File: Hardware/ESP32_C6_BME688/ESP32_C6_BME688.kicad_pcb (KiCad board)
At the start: 2 copper layers, 31.7 x 20 mm, 13 parts, among them J1 USB_C, J2 JST_PH_2PIN, J3 Daughterboard_Interface, U1 ESP32-C6-MINI-1, U3 MCP73831, U4 AP2112K-3.3

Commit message: working POC 1
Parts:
- moved R3 0.80 mm to (129.0, 102.0)
- moved R4 0.80 mm to (129.0, 105.5)
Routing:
- net CC1: track 15.6 -> 14.6 mm
- net GND: track 58.2 -> 57.5 mm
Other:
- board size 31.7 x 20 mm -> 30.8 x 20 mm
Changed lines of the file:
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@@
 	(footprint "Resistor_SMD:R_0603_1608Metric"
 		(layer "F.Cu")
-		(at 129.8 102 90)
+		(at 129 102 90)
 		(descr "Resistor SMD 0603 (1608 Metric), square (rectangular) end terminal, IPC-7351 nominal, (Body size source: IPC-SM-782 page 72, https://www.pcb-3d.com/wordpress/wp-content/uploads/ipc-sm-782a_amendment_1_and_2.pdf)")
 		(tags "resistor")
@@
 	(footprint "Resistor_SMD:R_0603_1608Metric"
 		(layer "F.Cu")
-		(at 129.8 105.5 90)
+		(at 129 105.5 90)
 		(descr "Resistor SMD 0603 (1608 Metric), square (rectangular) end terminal, IPC-7351 nominal, (Body size source: IPC-SM-782 page 72, https://www.pcb-3d.com/wordpress/wp-content/uploads/ipc-sm-782a_amendment_1_and_2.pdf)")
 		(tags "resistor")
@@
 			)
 		)
+		(model "${KICAD10_3DMODEL_DIR}/RF_Module.3dshapes/ESP32-C3-WROOM-02.step"
+			(hide yes)
+			(offset
+				(xyz 0 0 0)
+			)
+			(scale
+				(xyz 1 1 1)
+			)
+			(rotate
+				(xyz 0 0 0)
+			)
+		)
 	)
 	(footprint "Resistor_SMD:R_0603_1608Metric"
@@
 			)
 		)
+		(model "${KICAD10_3DMODEL_DIR}/Connector_USB.3dshapes/USB_C_Receptacle_GCT_USB4105-xx-A_16P_TopMnt_Horizontal.step"
+			(offset
+				(xyz 0 0 0)
+			)
+			(scale
+				(xyz 1 1 1)
+			)
+			(rotate
+				(xyz 0 0 0)
+			)
+		)
 	)
 	(gr_line
 		(start 100 100)
-		(end 131.699999 100)
+		(end 130.75 100)
 		(stroke
 			(width 0.1)
-			(type default)
+			(type solid)
 		)
 		(layer "Edge.Cuts")
@@
 	)
 	(gr_line
-		(start 131.699999 100)
-		(end 131.699999 120)
+		(start 130.75 100)
+		(end 130.75 120)
 		(stroke
 			(width 0.1)
-			(type default)
+			(type solid)
 		)
 		(layer "Edge.Cuts")
 	)
 	(gr_line
-		(start 131.699999 120)
+		(start 130.75 120)
 		(end 100 120)
 		(stroke
 			(width 0.1)
-			(type default)
+			(type solid)
 		)
 		(layer "Edge.Cuts")
@@
 	)
 	(segment
-		(start 123.6683 118.25)
-		(end 118.825 118.25)
+		(start 130.2 105.875)
+		(end 129 104.675)
 		(width 0.2)
 		(layer "F.Cu")
@@
 	)
 	(segment
-		(start 129.14 109.68)
-		(end 130.2917 109.68)
+		(start 123.6683 118.25)
+		(end 118.825 118.25)
 		(width 0.2)
 		(layer "F.Cu")
@@
 	)
 	(segment
-		(start 130.8329 102.2079)
-		(end 129.8 101.175)
-		(width 0.2)
-		(layer "F.Cu")
-		(net "GND")
-	)
-	(segment
 		(start 107.4 107.3)
 		(end 106.8 107.3)
@@
 	)
 	(segment
-		(start 130.576 103.8179)
-		(end 130.576 103.2144)
-		(width 0.15)
-		(layer "F.Cu")
-		(net "GND")
-	)
-	(segment
 		(start 102.5746 108.0729)
 		(end 105.175 108.0729)
@@
 	)
 	(segment
-		(start 130.2917 109.68)
-		(end 130.5775 109.3942)
+		(start 130.2 108.62)
+		(end 130.2 105.875)
 		(width 0.2)
 		(layer "F.Cu")
@@
 	)
 	(segment
-		(start 130.576 103.899)
-		(end 130.576 103.8179)
+		(start 130.2 102.375)
+		(end 129 101.175)
 		(width 0.2)
 		(layer "F.Cu")
@@
 	)
 	(segment
-		(start 130.5775 109.3942)
-		(end 130.5775 105.8257)
-		(width 0.2)
-		(layer "F.Cu")
-		(net "GND")
-	)
-	(segment
-		(start 129.8 104.675)
-		(end 130.576 103.899)
-		(width 0.2)
-		(layer "F.Cu")
-		(net "GND")
-	)
-	(segment
 		(start 114.4 107.3)
 		(end 115.7 106)
@@
 	)
 	(segment
-		(start 101.781 106.1173)
-		(end 101.781 103.4935)
+		(start 130.2 103.475)
+		(end 130.2 102.375)
 		(width 0.2)
 		(layer "F.Cu")
@@
 	)
 	(segment
-		(start 105.6481 107.5998)
-		(end 106.1541 107.5998)
+		(start 101.781 106.1173)
+		(end 101.781 103.4935)
 		(width 0.2)
 		(layer "F.Cu")
@@
 	)
 	(segment
-		(start 130.5775 105.8257)
-		(end 130.3758 105.624)
+		(start 105.6481 107.5998)
+		(end 106.1541 107.5998)
 		(width 0.2)
 		(layer "F.Cu")
@@
 	)
 	(segment
-		(start 130.576 103.2144)
-		(end 130.8329 102.9575)
-		(width 0.15)
-		(layer "F.Cu")
-		(net "GND")
-	)
-	(segment
 		(start 123.6683 110.0783)
 		(end 124.39 110.8)
@@
 	)
 	(segment
-		(start 130.3758 105.624)
-		(end 130.1756 105.624)
-		(width 0.15)
-		(layer "F.Cu")
-		(net "GND")
-	)
-	(segment
 		(start 123.6683 118.32)
 		(end 123.6683 118.25)
@@
 	)
 	(segment
-		(start 130.1756 105.624)
-		(end 129.8 105.2484)
-		(width 0.15)
+		(start 129.14 109.68)
+		(end 130.2 108.62)
+		(width 0.2)
 		(layer "F.Cu")
 		(net "GND")
 	)
 	(segment
-		(start 130.8329 102.9575)
-		(end 130.8329 102.2079)
+		(start 112.1625 118.25)
+		(end 111.9045 117.992)
 		(width 0.2)
 		(layer "F.Cu")
@@
 	)
 	(segment
-		(start 112.1625 118.25)
-		(end 111.9045 117.992)
+		(start 129 104.675)
+		(end 130.2 103.475)
 		(width 0.2)
 		(layer "F.Cu")
@@
 	)
 	(segment
-		(start 129.8 105.2484)
-		(end 129.8 104.675)
-		(width 0.2)
-		(layer "F.Cu")
-		(net "GND")
-	)
-	(segment
 		(start 101.2 107.5)
 		(end 102.0017 107.5)
@@
 	)
 	(segment
-		(start 128.8531 102.825)
-		(end 129.8 102.825)
-		(width 0.2)
-		(layer "F.Cu")
-		(net "CC1")
-	)
-	(segment
 		(start 127.45 104.2281)
 		(end 128.8531 102.825)
@@
 	)
 	(segment
-		(start 123.994 107.8128)
-		(end 128.3122 107.8128)
+		(start 129 107.125)
+		(end 129 106.325)
 		(width 0.2)
 		(layer "F.Cu")
@@
 	)
 	(segment
-		(start 124.39 112.25)
-		(end 123.1062 112.25)
+		(start 128.3122 107.8128)
+		(end 129 107.125)
 		(width 0.2)
 		(layer "F.Cu")
@@
 	)
 	(segment
-		(start 128.3122 107.8128)
-		(end 129.8 106.325)
+		(start 123.994 107.8128)
+		(end 128.3122 107.8128)
+		(width 0.2)
+		(layer "F.Cu")
+		(net "CC2")
+	)
+	(segment
+		(start 124.39 112.25)
+		(end 123.1062 112.25)
 		(width 0.2)
 		(layer "F.Cu")
@@
 		(polygon
 			(pts
-				(xy 99.5 99.5) (xy 132.199999 99.5) (xy 132.199999 120.5) (xy 99.5 120.5)
+				(xy 99.5 99.5) (xy 130.5 99.5) (xy 130.5 120.5) (xy 99.5 120.5)
 			)
 		)

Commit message: moved J3 to center of left edge
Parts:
- moved J3 1.21 mm to (101.0, 108.7)
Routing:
- net +3V3: track 29.4 -> 38.7 mm, vias 3 -> 6
- net I2C0_SCL: track 10.3 -> 17.9 mm
- net I2C0_SDA: track 24.0 -> 27.7 mm
- net GND: track 57.5 -> 56.1 mm

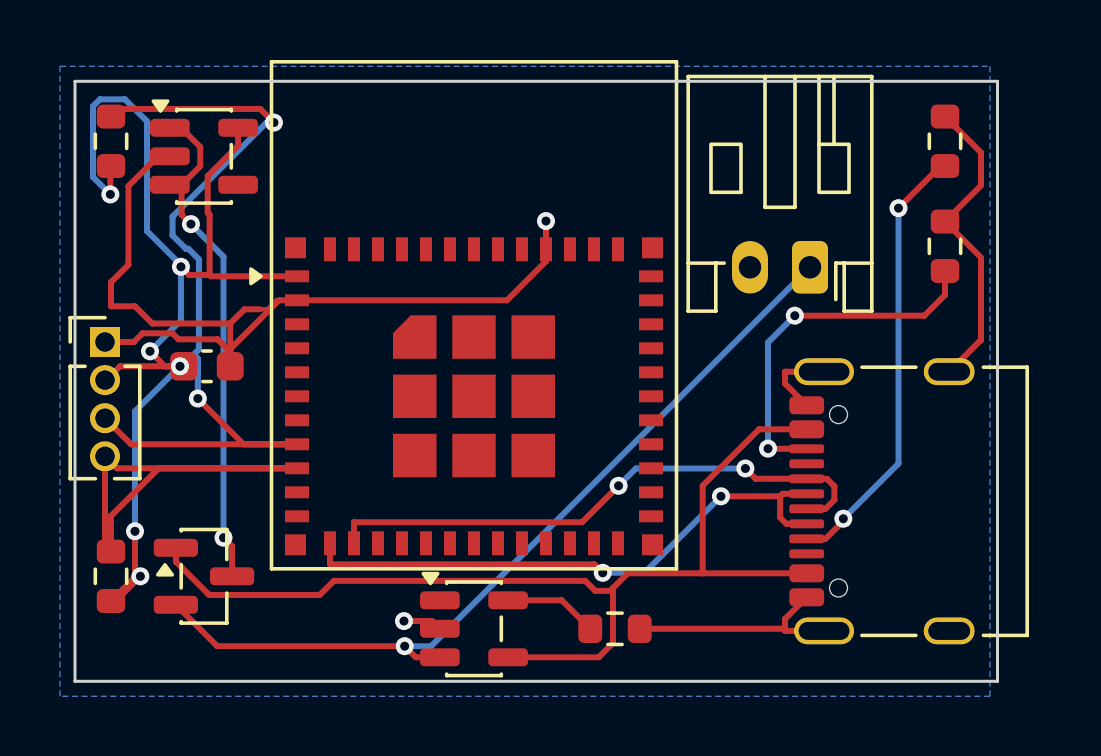
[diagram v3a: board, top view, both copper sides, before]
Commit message: compacted size
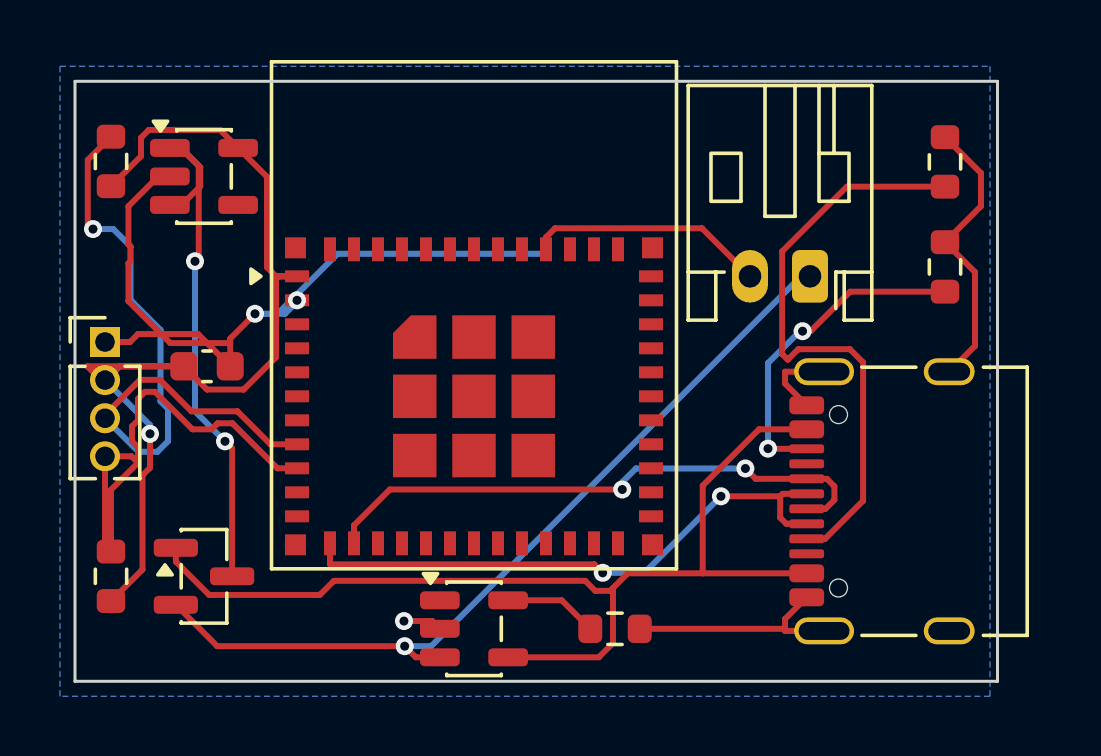
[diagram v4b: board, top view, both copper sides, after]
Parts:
- moved R3 0.69 mm to (129.0, 102.7)
- moved R4 0.69 mm to (129.0, 106.2)
- moved R1 0.67 mm to (101.2, 102.7)
- moved U4 0.67 mm to (104.3, 103.2)
- moved J2 0.30 mm to (124.5, 106.5)
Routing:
- net CC1: track 14.6 -> 19.9 mm, vias 2 -> 0
- net +3V3: track 38.7 -> 33.6 mm, vias 6 -> 1
- net I2C0_SDA: track 27.7 -> 22.7 mm, vias 2 -> 1
- net I2C0_SCL: track 17.9 -> 16.7 mm
- net CC2: track 12.2 -> 11.0 mm
- net VSYS: track 16.9 -> 17.9 mm
- net GND: track 56.1 -> 56.7 mm, vias 2 -> 3
